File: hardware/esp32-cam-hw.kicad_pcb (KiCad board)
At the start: 2 copper layers, 70 x 65 mm, 18 parts, among them J2 Conn_01x05_Pin, J3 Conn_01x04_Pin, J4 Conn_01x04_Pin, SW1 SW_Push, U2 Micro_USB_Converter

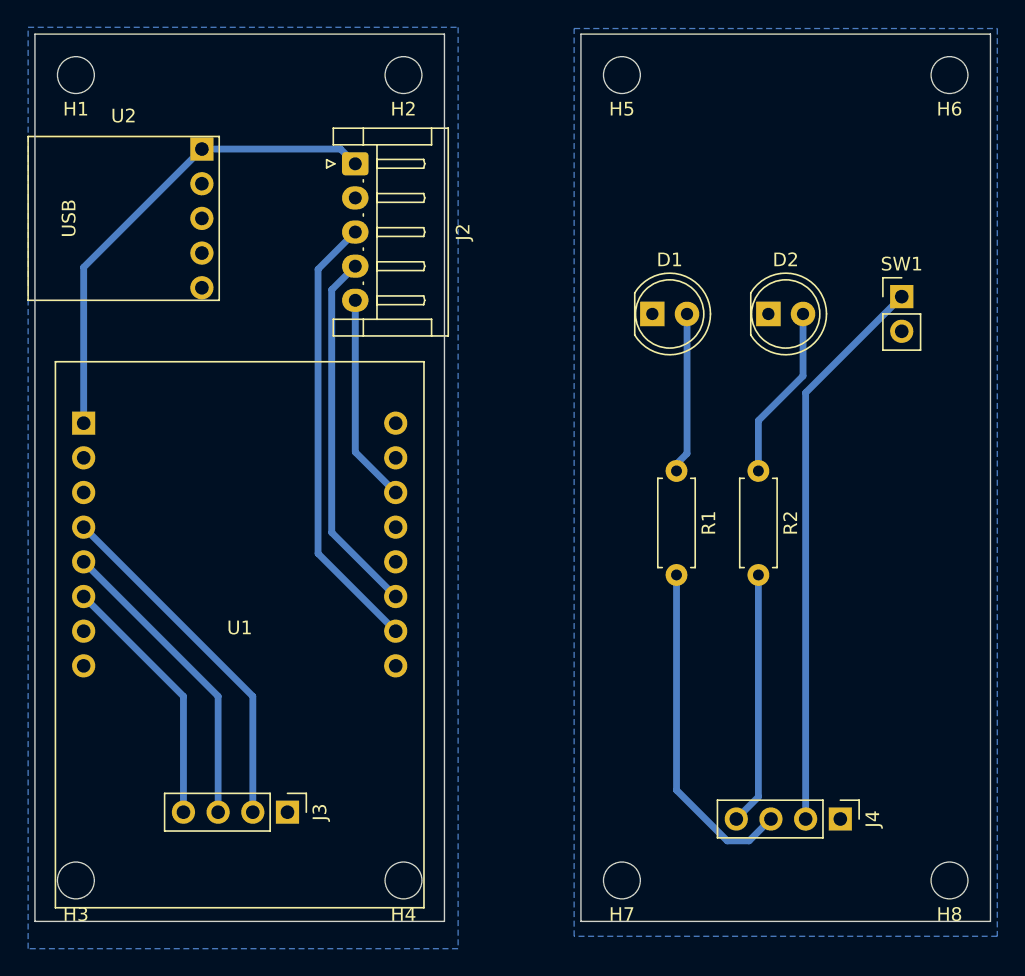
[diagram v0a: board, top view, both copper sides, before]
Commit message: Hardware: Center front panel components and add custom switch footprint
- Centered front panel components (SW1, D1, D2, J3, J4) precisely on the X-axis for optical symmetry.
- Added a custom KiCad footprint for the DTR 7/RT push button (9.5mm body, round).
- Adjusted THT pad sizes for the custom switch (2.6mm outer diameter, 2.0mm drill) to guarantee a minimum 0.6mm gap for CNC isolation milling.
- Updated README.md to reflect the specific switch model and adjusted PCB milling specifications.
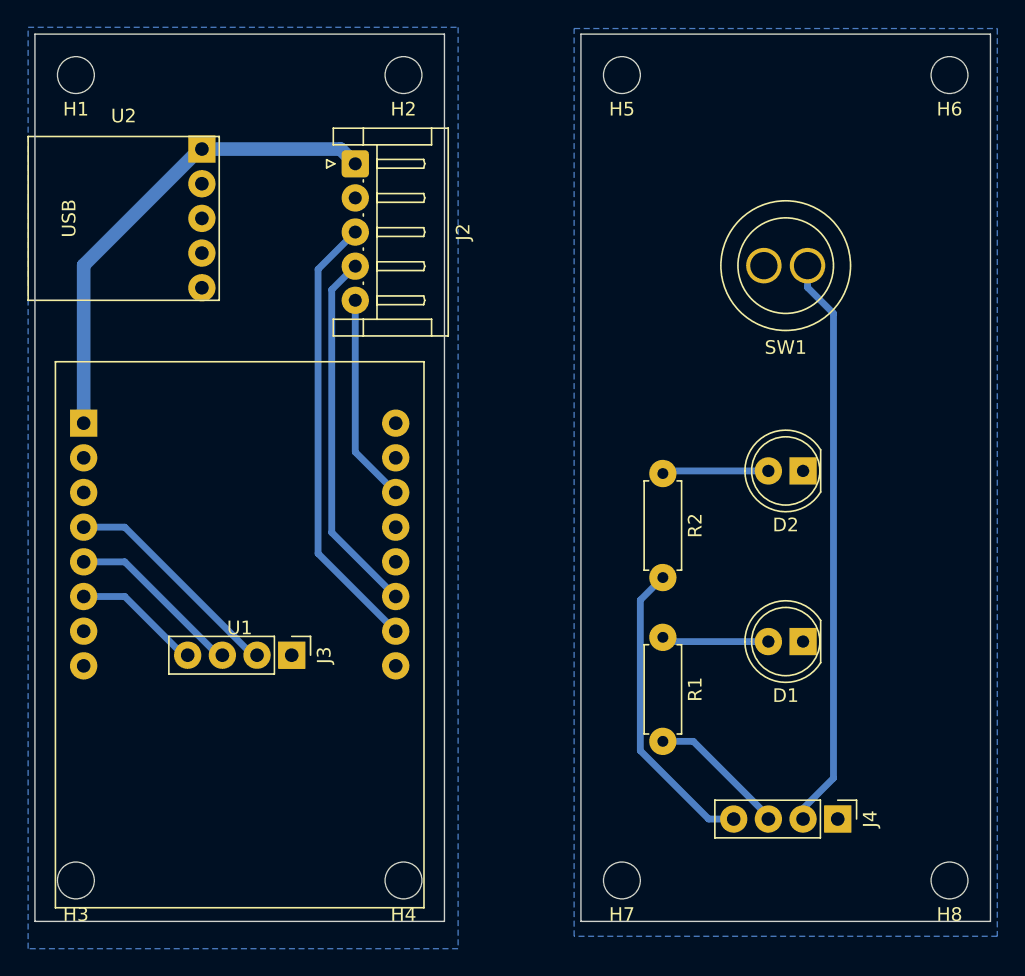
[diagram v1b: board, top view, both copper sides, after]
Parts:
- SW1: footprint Connector_PinHeader_2.54mm:PinHeader_1x02_P2.54mm_Vertical -> FootprintLibrary:SW_DTR_7_RT
- moved D1 26.4 mm to (169.8, 117.0), turned to 180 degrees
- moved R1 12.2 mm to (159.5, 116.7)
- moved D2 11.8 mm to (169.8, 104.5), turned to 180 degrees
- moved J3 11.5 mm to (132.3, 118.0)
- moved SW1 8.80 mm to (168.5, 89.5), turned to 180 degrees
- moved R2 7.00 mm to (159.5, 104.7)
- moved J4 0.19 mm to (172.3, 130.0)
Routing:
- net /FP_LED_ERROR: track 24.9 -> 10.3 mm
- net /LED_STATUS: track 18.8 -> 9.09 mm
- net /LED_ERROR: track 22.4 -> 12.7 mm
- net /TRIGGER: track 26.0 -> 16.3 mm
- net Net-(D2-A): track 12.9 -> 7.04 mm
- net Net-(D1-A): track 12.6 -> 7.09 mm
- net /FP_LED_STATUS: track 18.6 -> 22.5 mm

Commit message: Hardware: Replace antenna keepout zone with milling rectangle
- Removed the standard KiCad keepout zone under the ESP32-S antenna.
- Added a filled rectangle on the `Dwgs.User` (User.Drawings) layer to serve as a precise milling pocket for CNC isolation routing.
- Adjusted the GND copper polygon to perfectly avoid the antenna region.
- Updated README.md to document the new antenna cutout milling procedure.
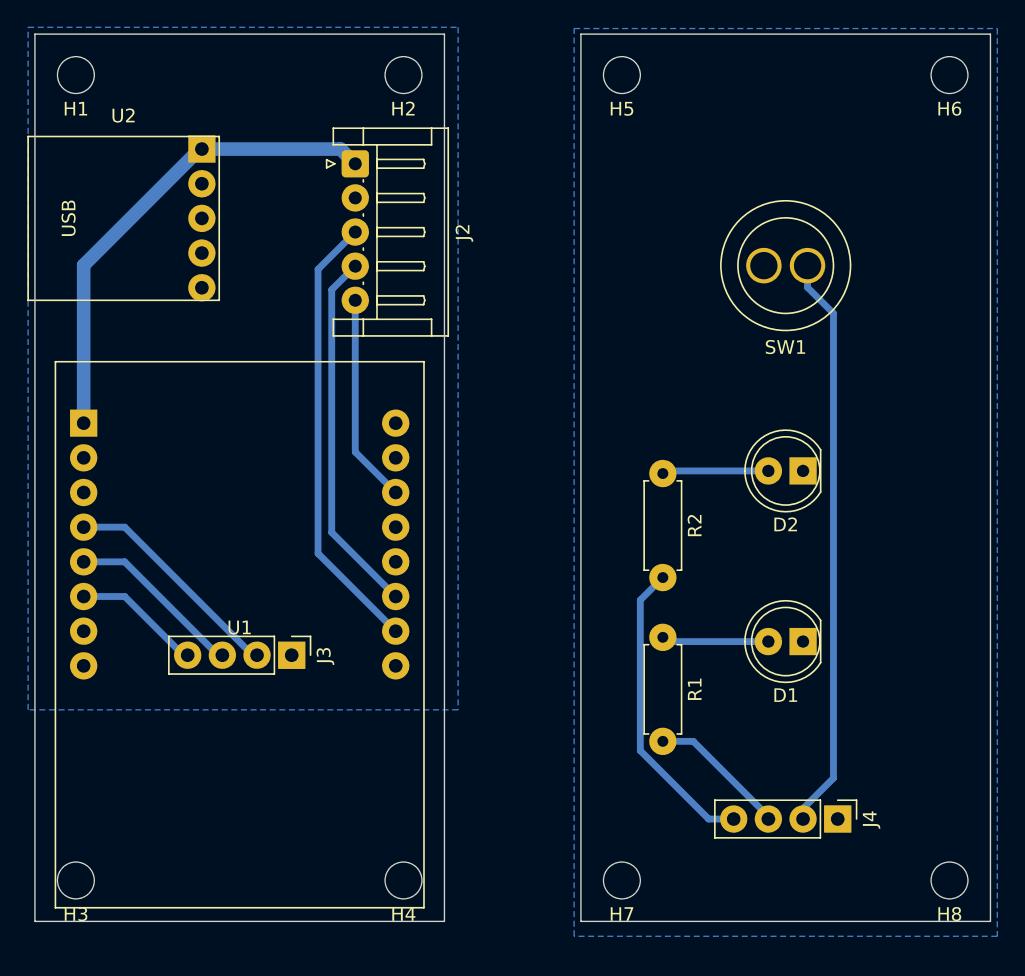
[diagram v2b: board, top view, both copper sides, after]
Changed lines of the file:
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@@
 		(grid_origin 116.5 134.5)
 		(pcbplotparams
-			(layerselection 0x00000000_00000000_55555555_57555554)
+			(layerselection 0x00000000_00000000_55555555_57575554)
 			(plot_on_all_layers_selection 0x00000000_00000000_00000000_00000000)
 			(disableapertmacros no)
@@
 	)
 	(gr_rect
+		(start 113.5 122.5)
+		(end 143.5 137.5)
+		(stroke
+			(width 0.2)
+			(type solid)
+		)
+		(fill yes)
+		(layer "Dwgs.User")
+	)
+	(gr_rect
 		(start 113.5 72.5)
 		(end 143.5 137.5)
@@
 		(polygon
 			(pts
-				(xy 113 72) (xy 144.5 72) (xy 144.5 139.5) (xy 113 139.5)
-			)
-		)
-	)
-	(zone
-		(net 0)
-		(net_name "")
-		(layer "B.Cu")
-		(name "Antenne")
-		(hatch edge 0.5)
-		(connect_pads
-			(clearance 0)
-		)
-		(min_thickness 0.25)
-		(filled_areas_thickness no)
-		(keepout
-			(tracks not_allowed)
-			(vias allowed)
-			(pads not_allowed)
-			(copperpour not_allowed)
-			(footprints not_allowed)
-		)
-		(placement
-			(enabled no)
-			(sheetname "/")
-		)
-		(fill
-			(thermal_gap 0.5)
-			(thermal_bridge_width 0.5)
-		)
-		(polygon
-			(pts
-				(xy 113 121.5) (xy 144.5 121.5) (xy 144.5 139.5) (xy 113 139.5)
+				(xy 113 72) (xy 144.5 72) (xy 144.5 122) (xy 113 122)
 			)
 		)
